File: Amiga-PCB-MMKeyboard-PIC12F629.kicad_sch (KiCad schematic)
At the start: 13 parts, among them J11 Amiga keyboard, J12 A500 mainboard, J2 PS/2 keyboard, SW500 SW_Push, U1 PIC12F629

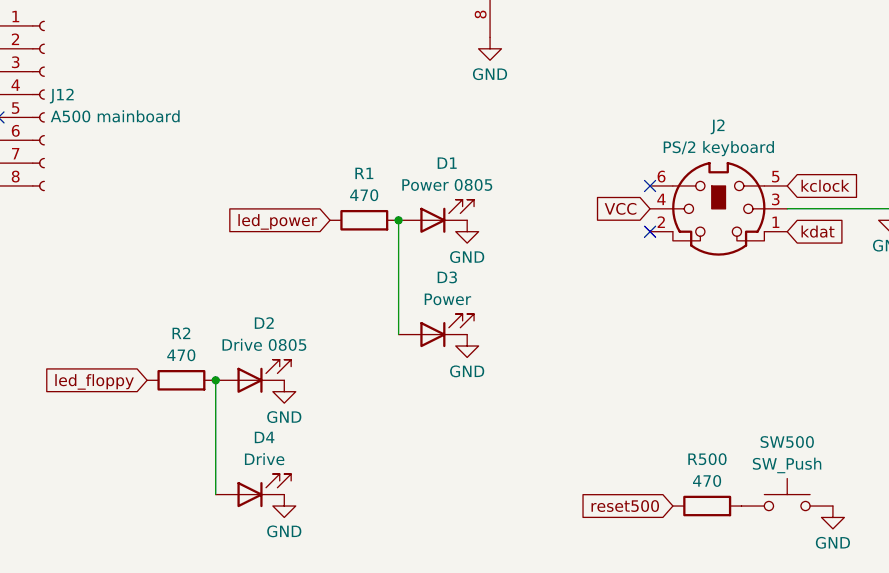
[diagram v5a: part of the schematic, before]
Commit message: v06: Sane LED resistor values depending on the LED's properties
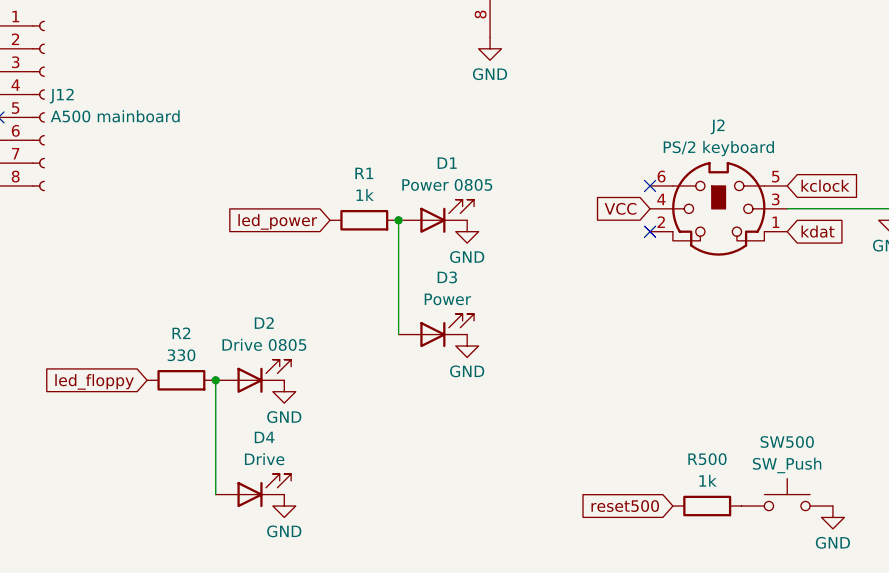
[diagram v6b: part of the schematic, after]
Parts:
- R1, R500: value 470 -> 1k; JLCPCB C17710 -> C17513; Reichelt SMD-0805 470 -> SMD-0805 1,00K
- R2: value 470 -> 330; JLCPCB C17710 -> C17630; Reichelt SMD-0805 470 -> SMD-0805 330
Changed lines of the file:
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@@
 		(fields_autoplaced yes)
 		(property "Reference" "R2"
-			(at 144.78 90.0897 90)
-			(effects
-				(font
-					(size 1.27 1.27)
-				)
-			)
-		)
-		(property "Value" "470"
-			(at 144.78 92.5139 90)
+			(at 144.78 90.0895 90)
+			(effects
+				(font
+					(size 1.27 1.27)
+				)
+			)
+		)
+		(property "Value" "330"
+			(at 144.78 92.5138 90)
 			(effects
 				(font
@@
 			)
 		)
-		(property "JLCPCB" "C17710"
+		(property "JLCPCB" "C17630"
 			(at 144.78 95.25 0)
 			(effects
@@
 			)
 		)
-		(property "Reichelt" "SMD-0805 470"
+		(property "Reichelt" "SMD-0805 330"
 			(at 144.78 95.25 0)
 			(effects
@@
 			)
 		)
-		(property "Value" "470"
+		(property "Value" "1k"
 			(at 203.2 106.4839 90)
 			(effects
@@
 			)
 		)
-		(property "JLCPCB" "C17710"
+		(property "JLCPCB" "C17513"
 			(at 203.2 109.22 0)
 			(effects
@@
 			)
 		)
-		(property "Reichelt" "SMD-0805 470"
+		(property "Reichelt" "SMD-0805 1,00K"
 			(at 203.2 109.22 0)
 			(effects
@@
 		(fields_autoplaced yes)
 		(property "Reference" "R1"
-			(at 165.1 72.3097 90)
-			(effects
-				(font
-					(size 1.27 1.27)
-				)
-			)
-		)
-		(property "Value" "470"
-			(at 165.1 74.7339 90)
+			(at 165.1 72.3095 90)
+			(effects
+				(font
+					(size 1.27 1.27)
+				)
+			)
+		)
+		(property "Value" "1k"
+			(at 165.1 74.7338 90)
 			(effects
 				(font
@@
 			)
 		)
-		(property "JLCPCB" "C17710"
+		(property "JLCPCB" "C17513"
 			(at 165.1 77.47 0)
 			(effects
@@
 			)
 		)
-		(property "Reichelt" "SMD-0805 470"
+		(property "Reichelt" "SMD-0805 1,00K"
 			(at 165.1 77.47 0)
 			(effects
